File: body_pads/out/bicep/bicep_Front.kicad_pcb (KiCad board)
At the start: 2 copper layers, 228.3 x 229 mm, 0 parts

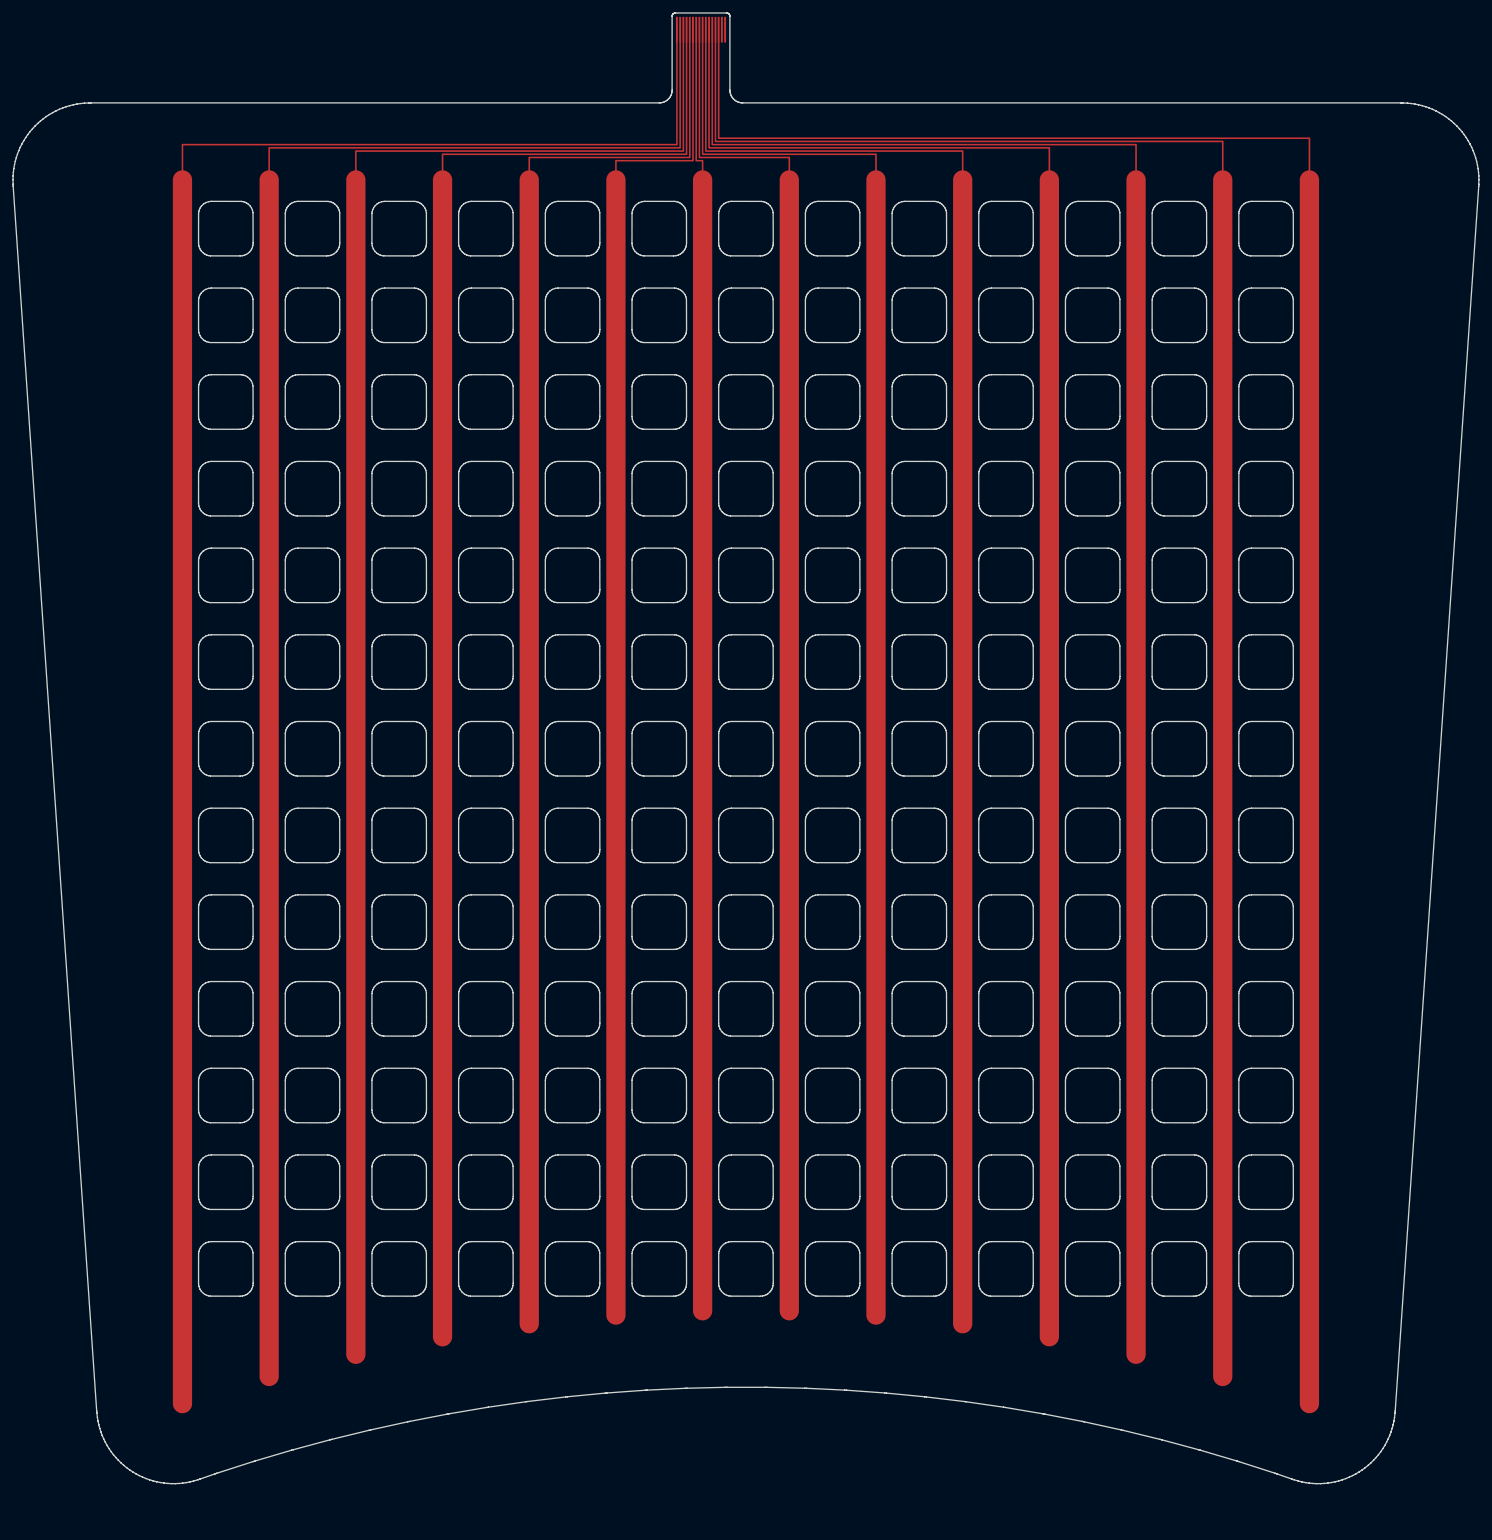
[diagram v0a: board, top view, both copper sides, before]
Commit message: Terminate body pads with vias and an FFC connector; export the full Gerber set
The pad tails now follow README Step 5 like the glove: every electrode trace
ends in a through via (0.45/0.2 mm, two staggered rows) and a 16-pin 0.5 mm
FFC connector (KiCad library Hirose FH12-16S-0.5SH) sits on the side opposite
the electrodes, making each board a 2-layer flex. A nested staircase fans the
0.5 mm bus out to the 1.0 mm via pitch and back to the 0.5 mm pads without
crossings. body_pads/kicad_post.py runs with KiCad's own python to add the
vias, footprint, connector-side tracks and nets; a .kicad_pro with flex rules
is written so kicad-cli DRC checks the right limits, and the Gerber export now
produces the same file set as the glove (both copper layers, mask, paste,
silkscreen, edge cuts, Eco1/Eco2, PTH/NPTH drills and maps).

Also: the column grid is shifted so no column exits under the tail bus, the
mirrored chest half swaps its tail order so both halves match, previews gain
a tail close-up, and the README describes the new tail, layers and checks.
Includes the body-pad documentation docx added to the working tree.

Co-Authored-By: Claude Fable 5.1 <noreply@anthropic.com>
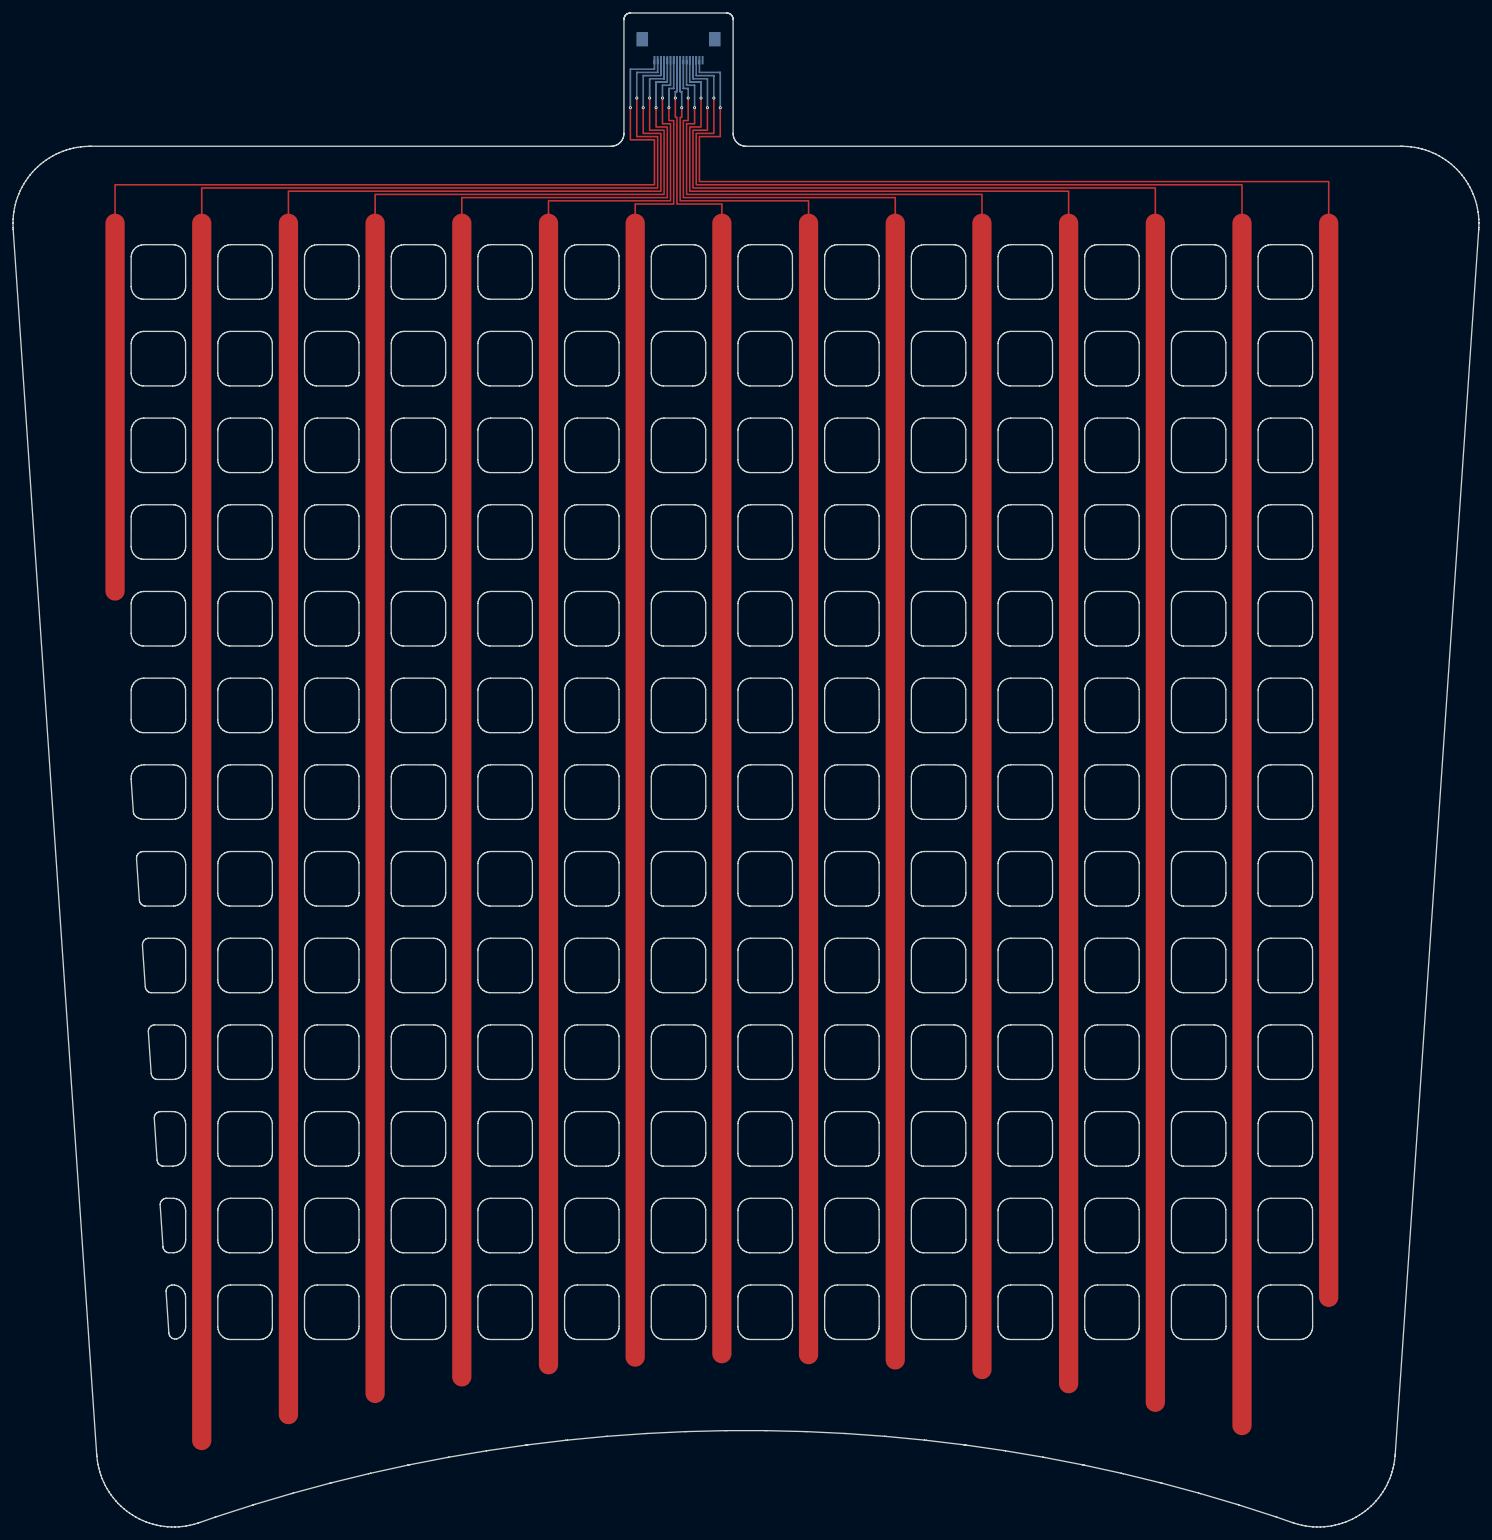
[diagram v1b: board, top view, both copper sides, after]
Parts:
- added J1: Hirose_FH12-16S-0.5SH_1x16-1MP_P0.50mm_Horizontal, Hirose_FH12-16S-0.5SH_1x16-1MP_P0.50mm_Horizontal, B.Cu at (113.6, 15.5)
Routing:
- net COL00: track 0.00 -> 11.2 mm, vias 0 -> 1
- net COL14: track 0.00 -> 10.7 mm, vias 0 -> 1
- net COL02: track 0.00 -> 10.2 mm, vias 0 -> 1
- net COL12: track 0.00 -> 9.65 mm, vias 0 -> 1
- net COL04: track 0.00 -> 9.15 mm, vias 0 -> 1
- net COL01: track 0.00 -> 9.15 mm, vias 0 -> 1
- net COL13: track 0.00 -> 8.65 mm, vias 0 -> 1
- net COL10: track 0.00 -> 8.65 mm, vias 0 -> 1
- net COL06: track 0.00 -> 8.15 mm, vias 0 -> 1
- net COL03: track 0.00 -> 8.15 mm, vias 0 -> 1
- net COL11: track 0.00 -> 7.65 mm, vias 0 -> 1
- net COL08: track 0.00 -> 7.65 mm, vias 0 -> 1
- net COL05: track 0.00 -> 7.15 mm, vias 0 -> 1
- net COL09: track 0.00 -> 6.65 mm, vias 0 -> 1
- net COL07: track 0.00 -> 6.15 mm, vias 0 -> 1
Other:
- board size 228.3 x 229 mm -> 228.3 x 235.8 mm
- board text added: "bicep Front"
- board text added: "bicep Front: 2-layer flex. Electrodes on F.Cu under the F.Mask opening; FFC connector J1 on B.Cu. Eco1.User = PSA adhesive on the F.Cu side. Eco2.User = stiffener under the connector (on the F.Cu side of the tail)."
- board text removed: "bicep Front: 1-layer flex, copper on F.Cu. F.Mask = coverlay openings. Eco1.User = PSA adhesive (copper side). Eco2.User = tail stiffener (opposite side), total tail 0.30 +/-0.05 mm. 16-pin 0.5 mm FFC fingers."

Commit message: Iteration 2: forearm pad from the measured paper template, bicep rescaled
The forearm outline is now digitised from the paper template wrapped round
the wearer's forearm (FOREARM_TEMPLATE_MM, scaled by the ruler in the photo):
240 mm round the arm at the elbow end, 210 mm long, narrowing to the 50 mm
underside strap at the wrist, tails on the elbow-end edge. The bicep pad is
scaled to the same arm (180 mm long, 200 -> 175 mm wide); the chest halves
are unchanged. Boards carry "iter2" in their title block and summary.json,
and all Gerbers, footprints, previews and checks are regenerated.

Also adds the template photos and the updated documentation docx.

Co-Authored-By: Claude Fable 5.1 <noreply@anthropic.com>
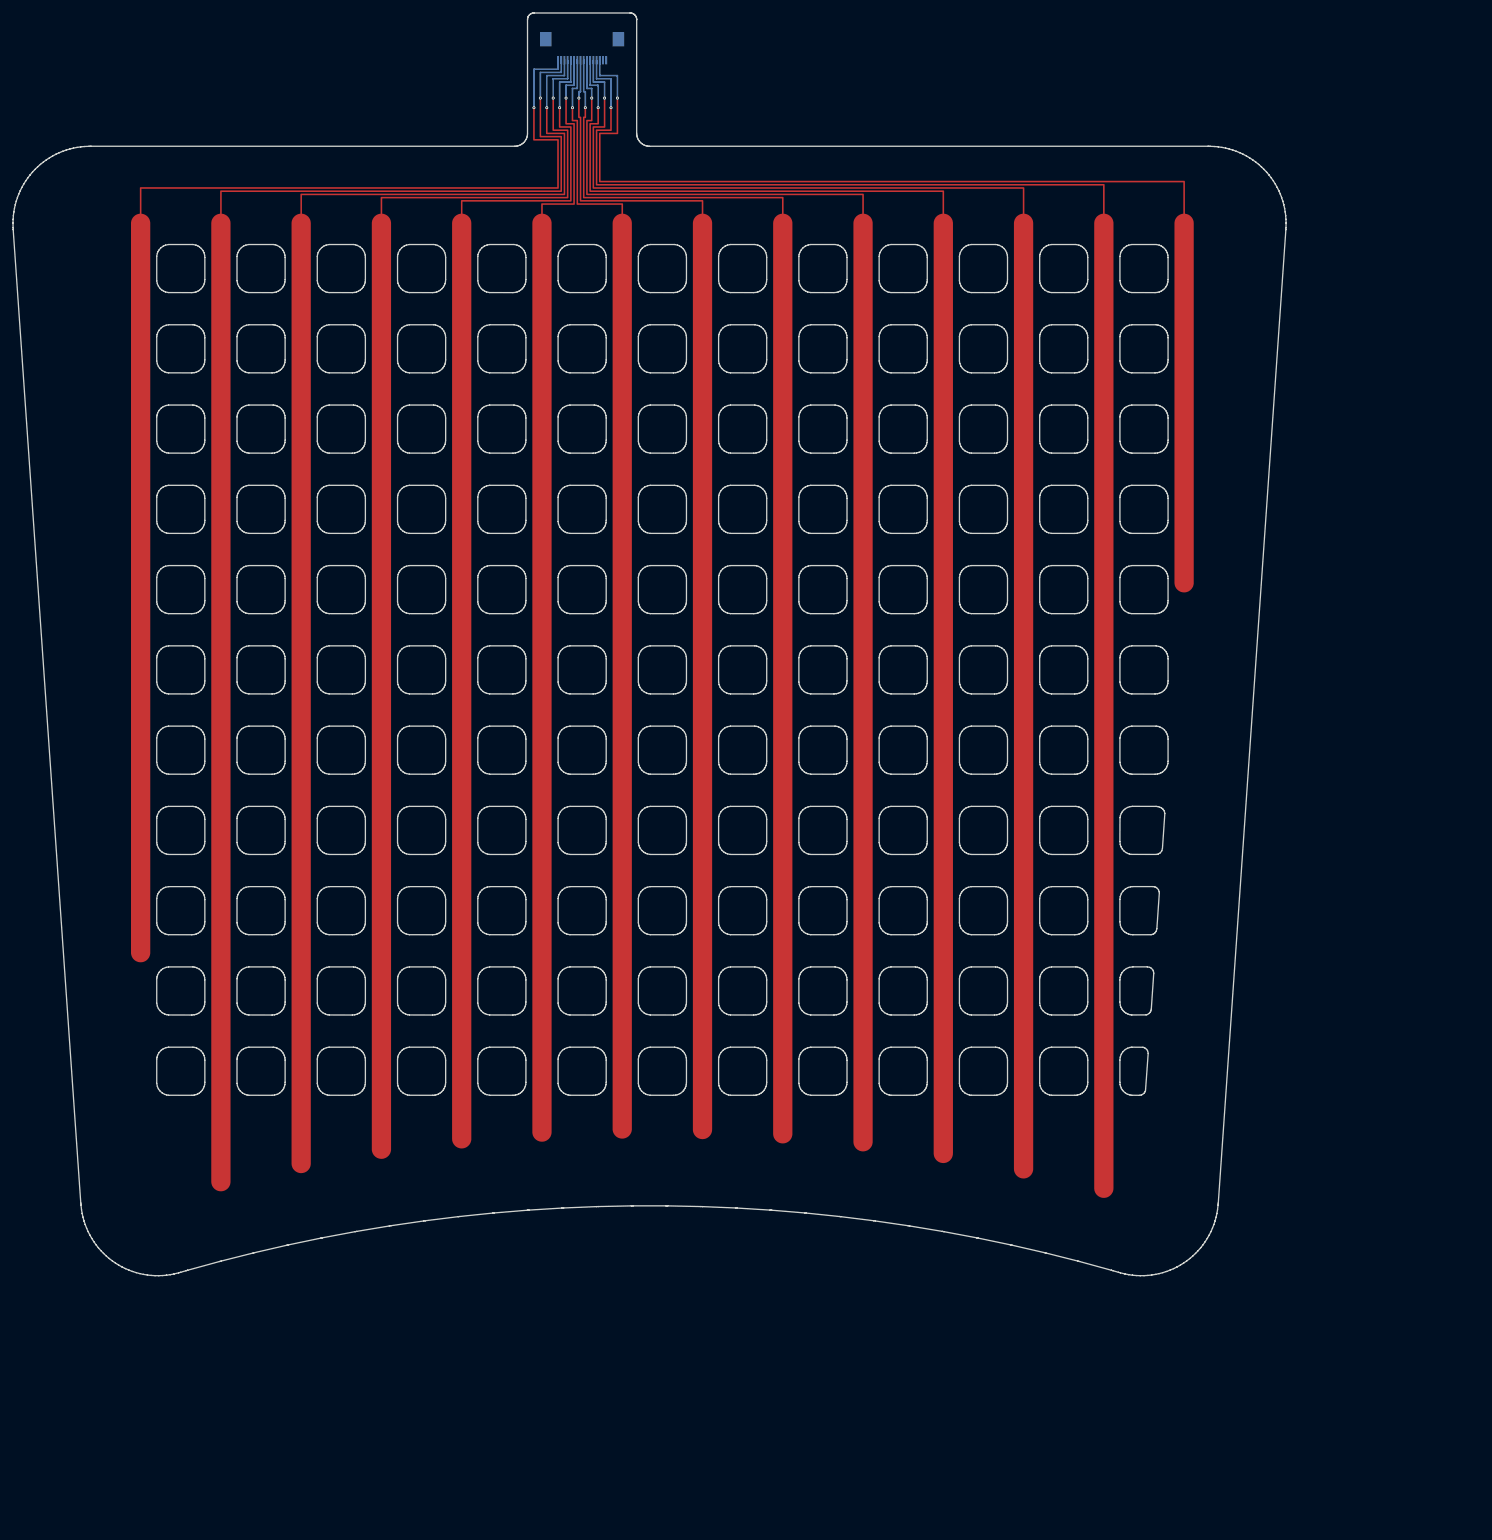
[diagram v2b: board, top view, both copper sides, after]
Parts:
- moved J1 15.0 mm to (98.6, 15.5)
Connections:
- J1 pad 15: COL14 -> (no net)
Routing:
- net COL14: track 10.7 -> 0.00 mm, vias 1 -> 0
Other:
- board size 228.3 x 235.8 mm -> 198.3 x 196.6 mm
